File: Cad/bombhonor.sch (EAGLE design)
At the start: 0 parts

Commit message: Aggiunti tutti i pezzi tranne il connettore batteria ed il pulsante, domani fine schematico e calcolo costo per sapere se si fa o si muore
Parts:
- added C1, C4: 10u, AlmaPASS:C1206
- added C2, C3, C5, C6, C7, C8: 0.1u, AlmaPASS:C0603
- added CN1: TC2030-MCP_SWD, AlmaCONN:TC2030-MCP_SWD
- added LED1, LED10, LED11, LED12, LED13, LED14, LED15, LED16, LED17, LED18, LED19, LED2, LED20, LED21, LED22, LED23, LED24, LED25, LED26, LED27, LED28, LED29, LED3, LED30, LED4, LED5, LED6, LED7, LED8, LED9: RED, AlmaOPTO:LED_SMD1206
- added R1, R10, R11, R12, R13, R14, R15, R16, R17, R18, R19, R2, R20, R21, R22, R23, R24, R25, R26, R27, R28, R29, R3, R30, R31, R32, R4, R5, R6, R7, R8, R9: 1k, AlmaPASS:R0603
- added U1: STM32F030F4, AlmaIC:STM32F030F4
- added U3: LDO_EN, AlmaDCDC:LDO_EN
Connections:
- new net +3V3: C1.1, C2.1, C4.1, C5.1, C6.1, C7.1, C8.1, CN1.VCC, U1.VDD, U1.VDDA, U3.VOUT
- new net +5V: U3.VIN
- new net GND: C1.2, C2.2, C3.2, C4.2, C5.2, C6.2, C7.2, C8.2, CN1.GND, LED1.K, LED10.K, LED11.K, LED12.K, LED13.K, LED14.K, LED15.K, LED16.K, LED17.K, LED18.K, LED19.K, LED2.K, LED20.K, LED21.K, LED22.K, LED23.K, LED24.K, LED25.K, LED26.K, LED27.K, LED28.K, LED29.K, LED3.K, LED30.K, LED4.K, LED5.K, LED6.K, LED7.K, LED8.K, LED9.K, R32.2, U1.BOOT0, U1.VSS, U3.GND
- new net LED1: R1.2, R11.2, R16.2, R21.2, R26.2, R6.2, U1.PA2
- new net LED2: R12.2, R17.2, R2.2, R22.2, R27.2, R7.2, U1.PA3
- new net LED3: R13.2, R18.2, R23.2, R28.2, R3.2, R8.2, U1.PA4
- new net LED4: R14.2, R19.2, R24.2, R29.2, R4.2, R9.2, U1.PA5
- new net LED5: R10.2, R15.2, R20.2, R25.2, R30.2, R5.2, U1.PA6
- new net N$1: LED1.A, R1.1
- new net N$10: LED10.A, R10.1
- new net N$11: LED11.A, R11.1
- new net N$12: LED12.A, R12.1
- new net N$13: LED13.A, R13.1
- new net N$14: LED14.A, R14.1
- new net N$15: LED15.A, R15.1
- new net N$16: LED16.A, R16.1
- new net N$17: LED17.A, R17.1
- new net N$18: LED18.A, R18.1
- new net N$19: LED19.A, R19.1
- new net N$2: LED2.A, R2.1
- new net N$20: LED20.A, R20.1
- new net N$21: LED21.A, R21.1
- new net N$22: LED22.A, R22.1
- new net N$23: LED23.A, R23.1
- new net N$24: LED24.A, R24.1
- new net N$25: LED25.A, R25.1
- new net N$26: LED26.A, R26.1
- new net N$27: LED27.A, R27.1
- new net N$28: LED28.A, R28.1
- new net N$29: LED29.A, R29.1
- new net N$3: LED3.A, R3.1
- new net N$30: LED30.A, R30.1
- new net N$32: R31.1, R32.1, U3.ENABLE
- new net N$4: LED4.A, R4.1
- new net N$5: LED5.A, R5.1
- new net N$6: LED6.A, R6.1
- new net N$7: LED7.A, R7.1
- new net N$8: LED8.A, R8.1
- new net N$9: LED9.A, R9.1
- new net NRST: C3.1, CN1.NRESET, U1.NRST
- new net ON: R31.2, U1.PA9
- new net SWCLK: CN1.SWCLK, U1.PA14
- new net SWDIO: CN1.SWDIO, U1.PA13
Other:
- note added: "portabatteria BK-883-TR, pulsante TR1-01"

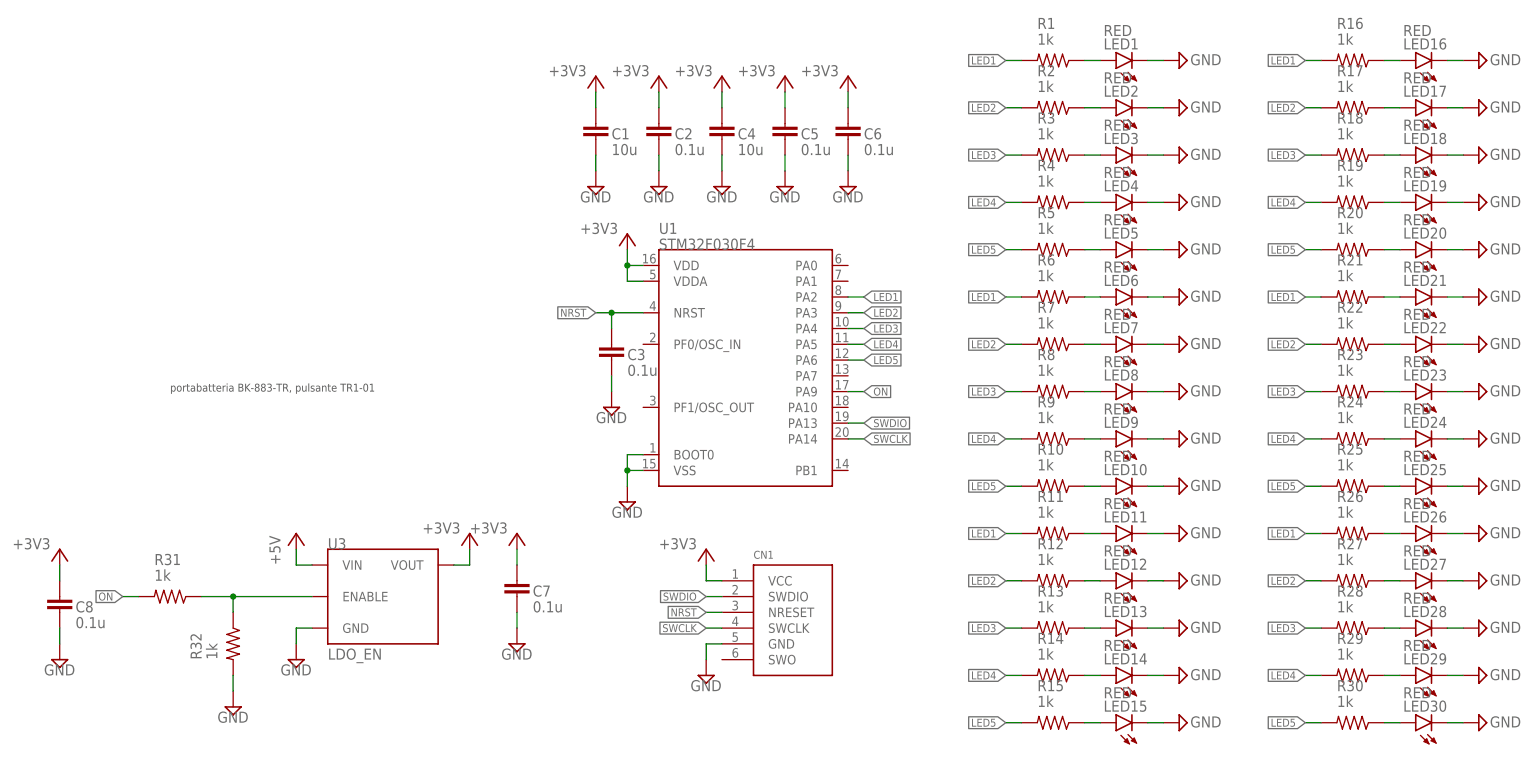
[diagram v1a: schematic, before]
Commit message: Finito lo schematico. Mancano i parno per i passivi.
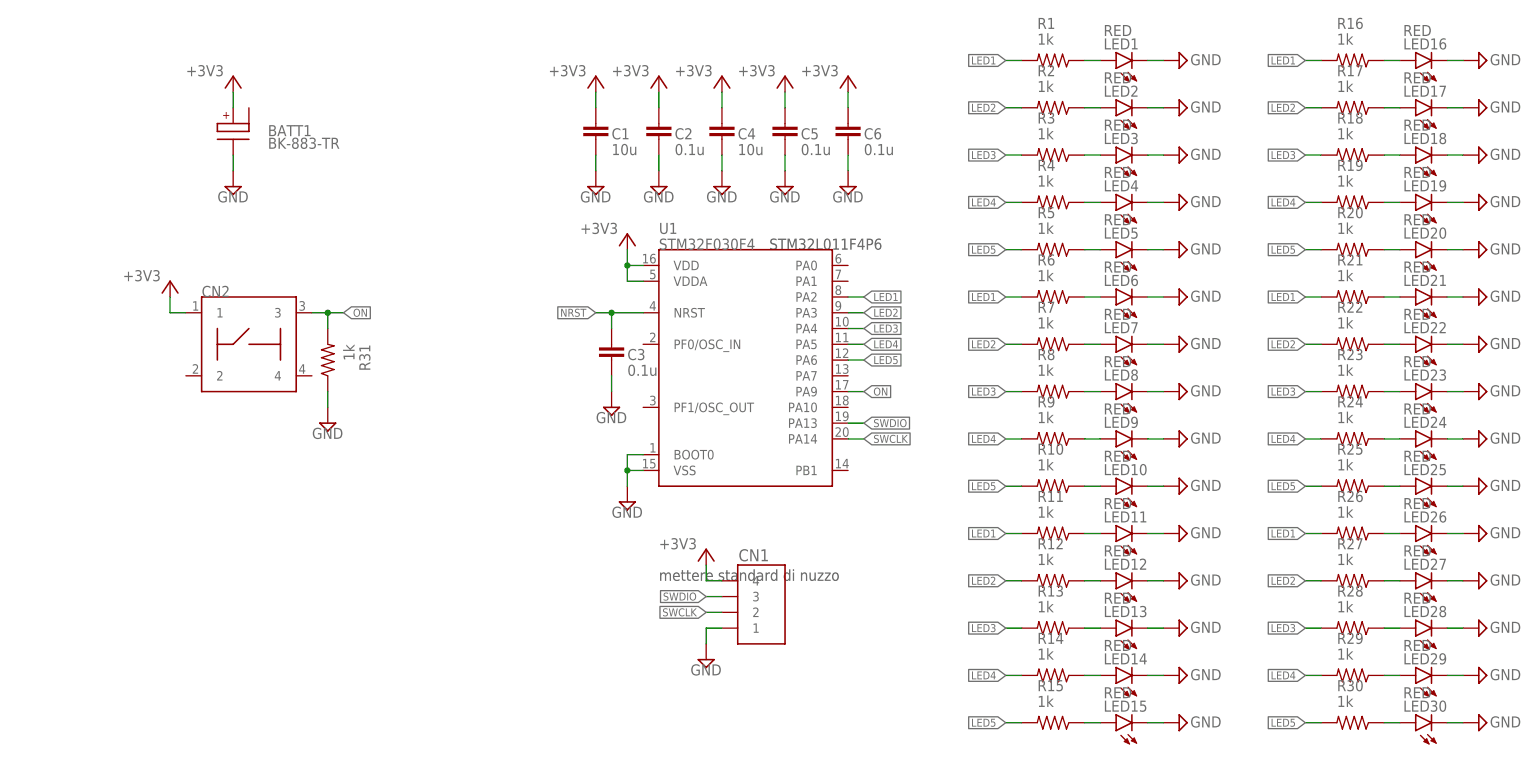
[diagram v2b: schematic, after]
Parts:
- removed C7, C8: 0.1u, AlmaPASS:C0603
- removed R32: 1k, AlmaPASS:R0603
- removed U3: LDO_EN, AlmaDCDC:LDO_EN
- added BATT1: BK-883-TR, AlmaBATT:BK-883-TR
- added CN2: TR1-01, cesso:TR1-01
- CN1: value TC2030-MCP_SWD -> HEADER4X1_2MM_SMD; device AlmaCONN:TC2030-MCP_SWD -> AlmaCONN:HEADER4X1_2MM_SMD; PARTNO DNP -> 2PH1-04-UA-SMT-B
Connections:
- removed net +5V: U3.VIN
- removed net N$32: R31.1, R32.1, U3.ENABLE
- net +3V3: now also BATT1.V_BATT1, CN1.4, CN2.1; no longer C7.1, C8.1, CN1.VCC, U3.VOUT
- net GND: now also BATT1.GND, CN1.1, R31.1; no longer C7.2, C8.2, CN1.GND, R32.2, U3.GND
- net NRST: no longer CN1.NRESET
- net ON: now also CN2.3
- net SWCLK: now also CN1.2; no longer CN1.SWCLK
- net SWDIO: now also CN1.3; no longer CN1.SWDIO
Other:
- note added: "STM32L011F4P6"
- note added: "mettere standard di nuzzo"
- note removed: "portabatteria BK-883-TR, pulsante TR1-01"
- moved on the sheet: R31

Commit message: Finito lo sbroglio della scheda
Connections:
- net +3V3: now also BATT1.V_BATT2; no longer BATT1.V_BATT1
- net LED1: now also U1.PA0; no longer U1.PA2
- net LED2: now also U1.PA1; no longer U1.PA3
- net LED3: now also U1.PA2; no longer U1.PA4
- net LED4: now also U1.PA3; no longer U1.PA5
- net LED5: now also U1.PA4; no longer U1.PA6
- net ON: now also U1.PF0/OSC_IN; no longer U1.PA9

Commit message: Terminata la BOM, da calcolare la spesa totale
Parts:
- C1, C4: device AlmaPASS:C1206 -> AlmaPASS:C0805; PARTNO (none) -> CL21A106KQCLRNC
- C2, C3, C5, C6: PARTNO (none) -> CL10B104KB8NNNC
- R1, R10, R11, R12, R13, R14, R15, R16, R17, R18, R19, R2, R20, R21, R22, R23, R24, R25, R26, R27, R28, R29, R3, R30, R31, R4, R5, R6, R7, R8, R9: PARTNO (none) -> RMCF0603JT1K00

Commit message: Messe a posto le piste
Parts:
- U1: PARTNO STM32F030F4P6TR -> STM32L011F4P6
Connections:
- net LED1: now also U1.PA4; no longer U1.PA0
- net LED2: now also U1.PA3; no longer U1.PA1
- net LED4: now also U1.PA1; no longer U1.PA3
- net LED5: now also U1.PA0; no longer U1.PA4

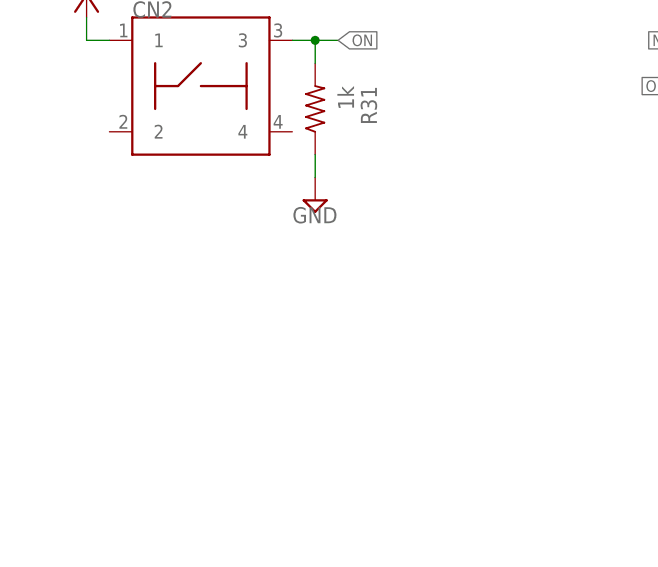
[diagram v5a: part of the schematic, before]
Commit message: Aggiunto firmware base che si illumina. Messa a posto la bom e scritto commenti con partno sullo schematico
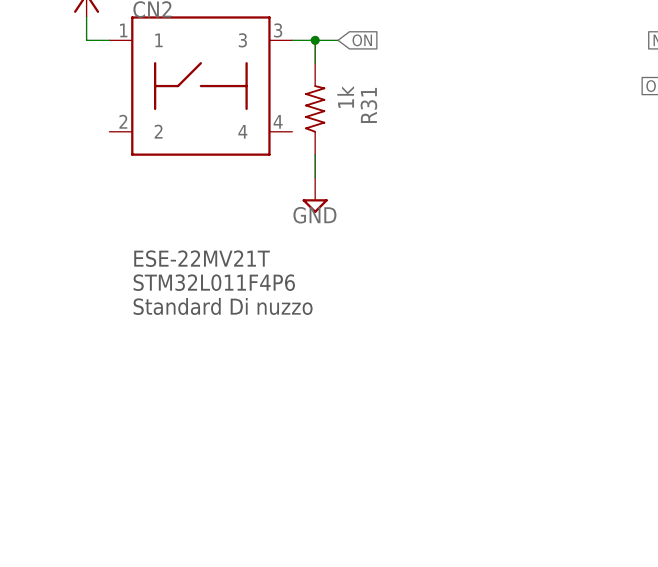
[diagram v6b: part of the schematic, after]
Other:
- note added: "ESE-22MV21T STM32L011F4P6 Standard Di nuzzo"
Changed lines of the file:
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@@
 <text x="132.08" y="137.16" size="1.778" layer="97">STM32L011F4P6</text>
 <text x="114.3" y="83.82" size="1.778" layer="97">mettere standard di nuzzo</text>
+<text x="40.64" y="96.52" size="1.778" layer="97">ESE-22MV21T
+STM32L011F4P6
+Standard Di nuzzo</text>
 </plain>
 <instances>
@@
 </schematic>
 </drawing>
+<compatibility>
+<note version="6.3" minversion="6.2.2" severity="warning">
+Since Version 6.2.2 text objects can contain more than one line,
+which will not be processed correctly with this version.
+</note>
+</compatibility>
 </eagle>

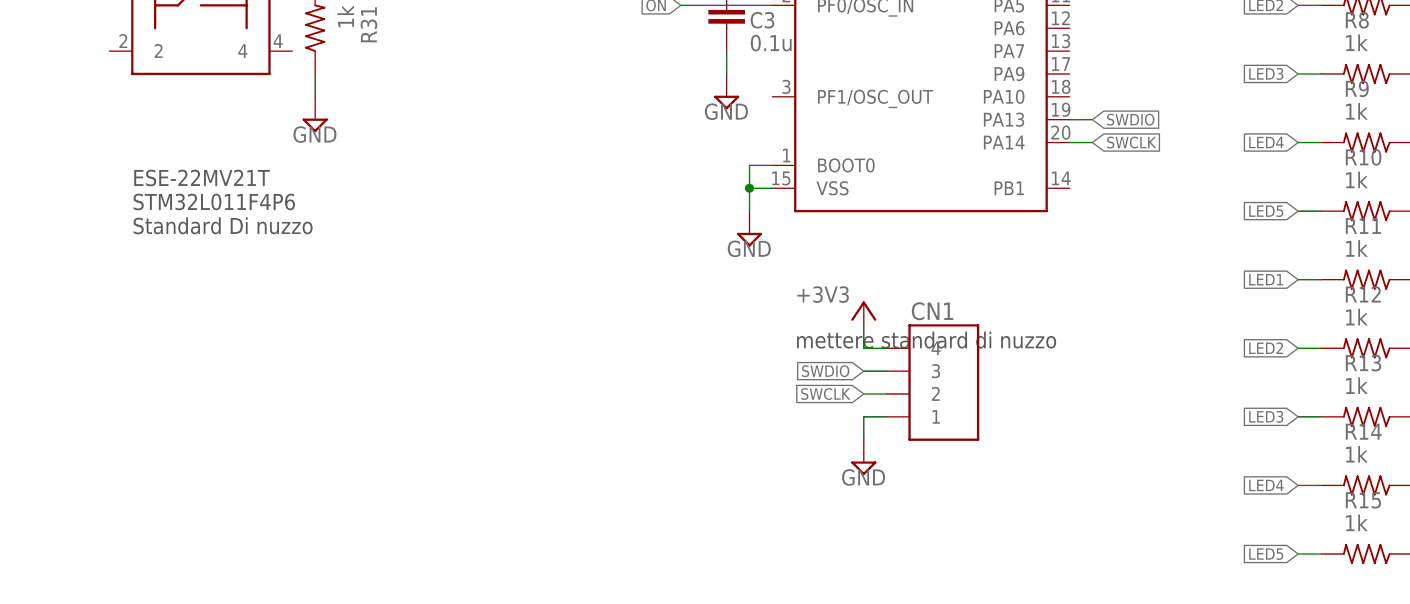
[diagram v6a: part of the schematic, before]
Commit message: Aggiunte cose da comprare allo schematico Ridotto la velocità di blinking nel FW
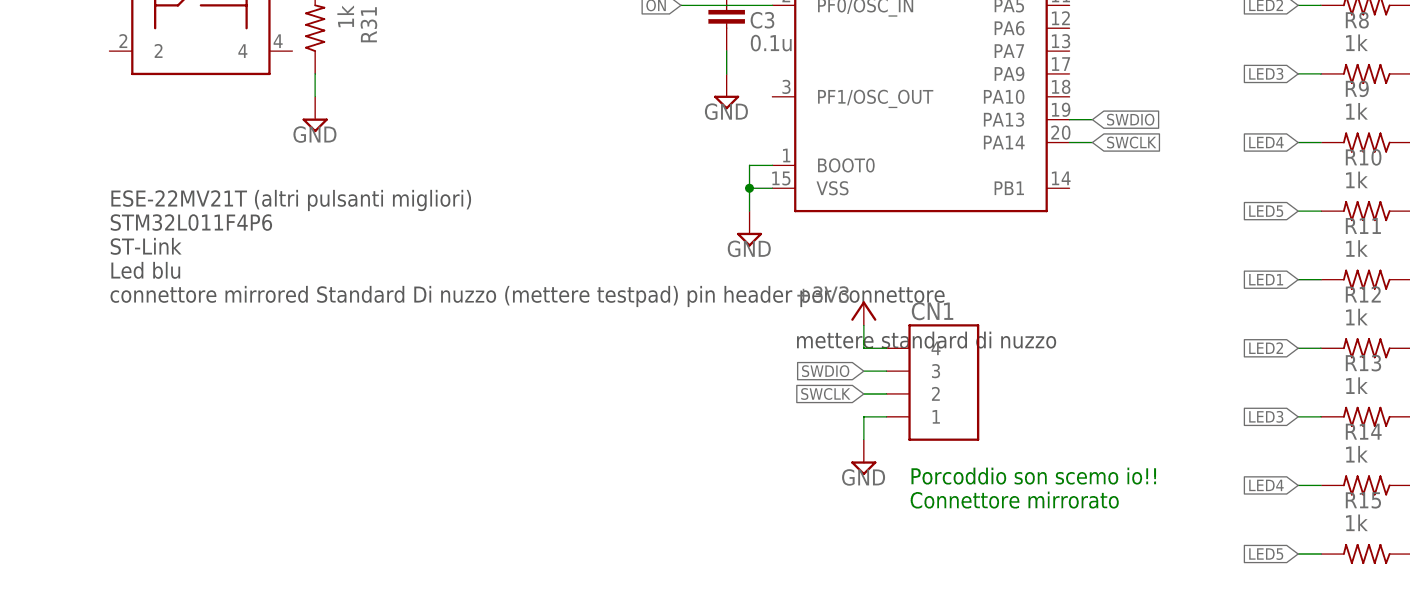
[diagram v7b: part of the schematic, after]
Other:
- note added: "ESE-22MV21T (altri pulsanti migliori) STM32L011F4P6 ST-Link Led blu connettore mirrored Standard Di nuzzo (mettere testpad) pin header per connettore"
- note added: "Porcoddio son scemo io!! Connettore mirrorato"
- note removed: "ESE-22MV21T STM32L011F4P6 Standard Di nuzzo"
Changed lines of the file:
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@@
 <text x="132.08" y="137.16" size="1.778" layer="97">STM32L011F4P6</text>
 <text x="114.3" y="83.82" size="1.778" layer="97">mettere standard di nuzzo</text>
-<text x="40.64" y="96.52" size="1.778" layer="97">ESE-22MV21T
+<text x="38.1" y="88.9" size="1.778" layer="97">ESE-22MV21T (altri pulsanti migliori)
 STM32L011F4P6
-Standard Di nuzzo</text>
+ST-Link
+Led blu
+connettore mirrored Standard Di nuzzo (mettere testpad) pin header per connettore
+</text>
+<text x="127" y="66.04" size="1.778" layer="91">Porcoddio son scemo io!!
+Connettore mirrorato</text>
 </plain>
 <instances>
